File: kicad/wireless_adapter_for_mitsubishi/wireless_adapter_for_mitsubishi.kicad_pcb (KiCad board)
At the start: 2 copper layers, 75 x 50 mm, 53 parts, among them J1 S05B-PASK-2(LF)(SN), J2 S05B-PASK-2(LF)(SN), J3 GT-USB-7010ASV, U1 ESP32-C6-WROOM-1-N8, U2 TXS0104EPWR, U3 TVS1400DRVR, U4 TVS0500DRVR, U5 TVS1400DRVR, U6 TVS0500DRVR, U7 TPS2121RUXR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

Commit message: Rename some of the KiCad sheets.
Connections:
- net /Power Regulator/Power_Multiplexed renamed /Power System/Power_Multiplexed
- net /Power Regulator/Regulator_Input renamed /Power System/Regulator_Input
- net /Power Regulator/USB_5V renamed /Power System/USB_5V

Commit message: Fix the name of a KiCad sheet.
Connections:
- net /Power System/Power_Multiplexed renamed /Power Subsystem/Power_Multiplexed
- net /Power System/Regulator_Input renamed /Power Subsystem/Regulator_Input
- net /Power System/USB_5V renamed /Power Subsystem/USB_5V

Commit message: Rename some KiCad buses.
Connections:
- net /IU Connector/IU_RX_WA_TX renamed /IU Connector/IU_UART_RX
- net /IU Connector/IU_TX_WA_RX renamed /IU Connector/IU_UART_TX
- net /WR Connector/WR_RX_WA_TX renamed /WR Connector/WR_UART_RX
- net /WR Connector/WR_TX_WA_RX renamed /WR Connector/WR_UART_TX

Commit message: Clean up KiCad schematic.
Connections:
- net /Power Subsystem/Power_Multiplexed renamed /Power Subsystem/Multiplexer_Output
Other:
- board text added: "Wireless Adapter for a Mitsubishi Heat Pump Indoor Unit (Rev: 1.1)"
- board text removed: "Wireless Adapter for a Mitsubishi Heat Pump Indoor Unit"

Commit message: Flatten KiCad schematic.
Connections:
- net /IU Connector/IU_12V7 renamed /IU_12V7
- net /IU Connector/IU_5V renamed /IU_5V
- net /IU Connector/IU_UART_RX renamed Net-(U2-A2)
- net /IU Connector/IU_UART_TX renamed Net-(U2-A1)
- net /Power Subsystem/Multiplexer_Output renamed /Multiplexer_Output
- net /Power Subsystem/Regulator_Input renamed /Regulator_Input
- net /Power Subsystem/USB_5V renamed /USB_5V
- net /WR Connector/WR_UART_RX renamed Net-(U2-A3)
- net /WR Connector/WR_UART_TX renamed Net-(U2-A4)

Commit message: Clean up KiCad schematic.
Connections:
- net Net-(U2-A1) renamed /IU_UART_TX
- net Net-(U2-A2) renamed /IU_UART_RX
- net Net-(U2-A3) renamed /WR_UART_RX
- net Net-(U2-A4) renamed /WR_UART_TX

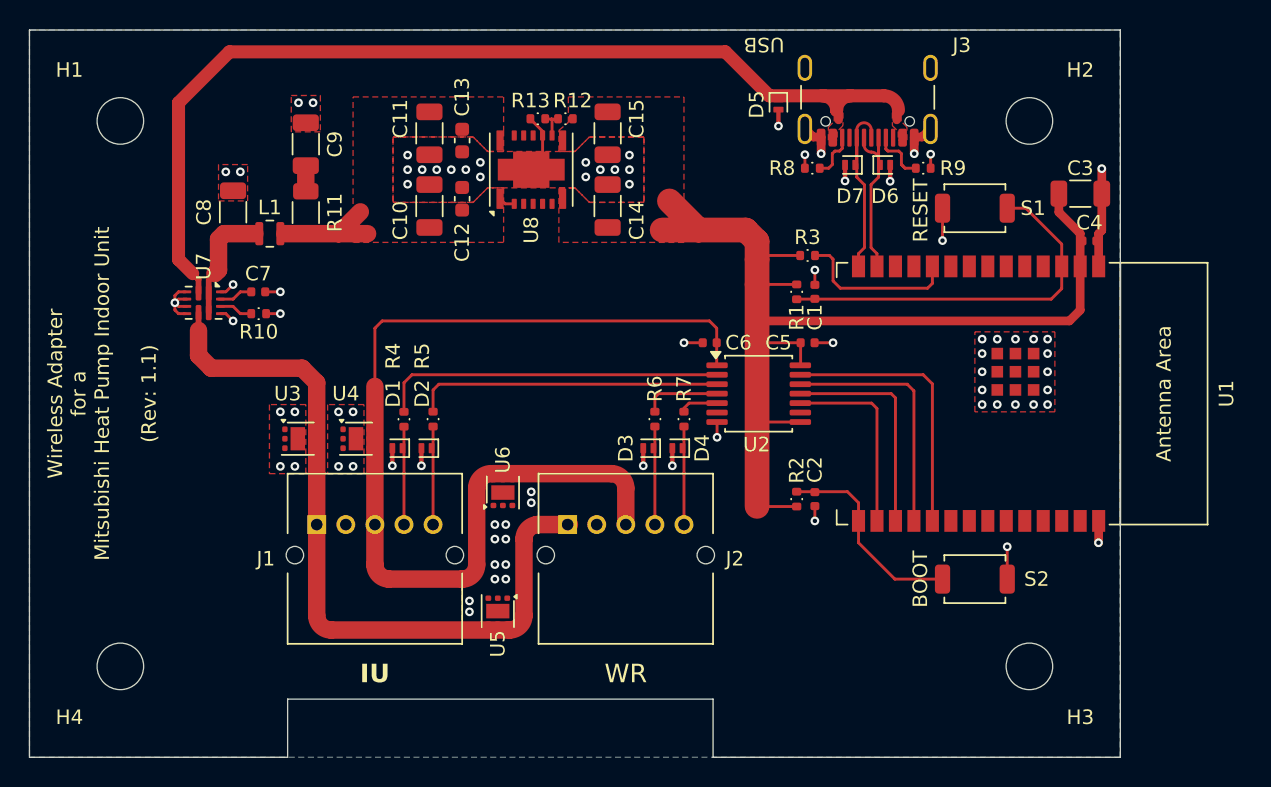
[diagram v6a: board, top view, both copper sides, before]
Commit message: Clean up KiCad schematic. Improve grounding in on PCB.
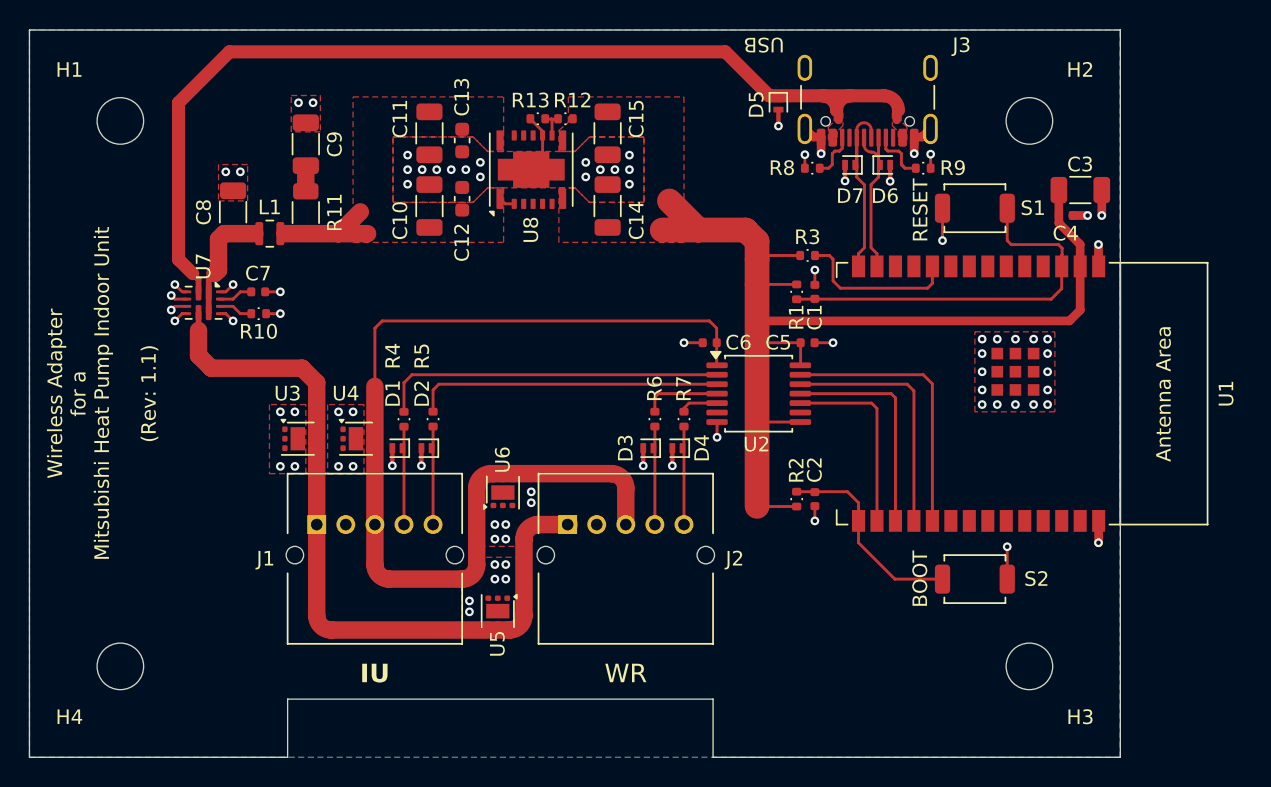
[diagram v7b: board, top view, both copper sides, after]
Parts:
- C2: value 1μF -> 0.1μF
- S1, S2: value SW_SPST -> SW_PUSH
- moved C4 2.39 mm to (171.2, 87.8)
- moved C3 0.25 mm to (172.2, 86.0)
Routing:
- net GND: track 45.3 -> 42.6 mm, vias 81 -> 86
- net /RESET: track 26.3 -> 27.5 mm

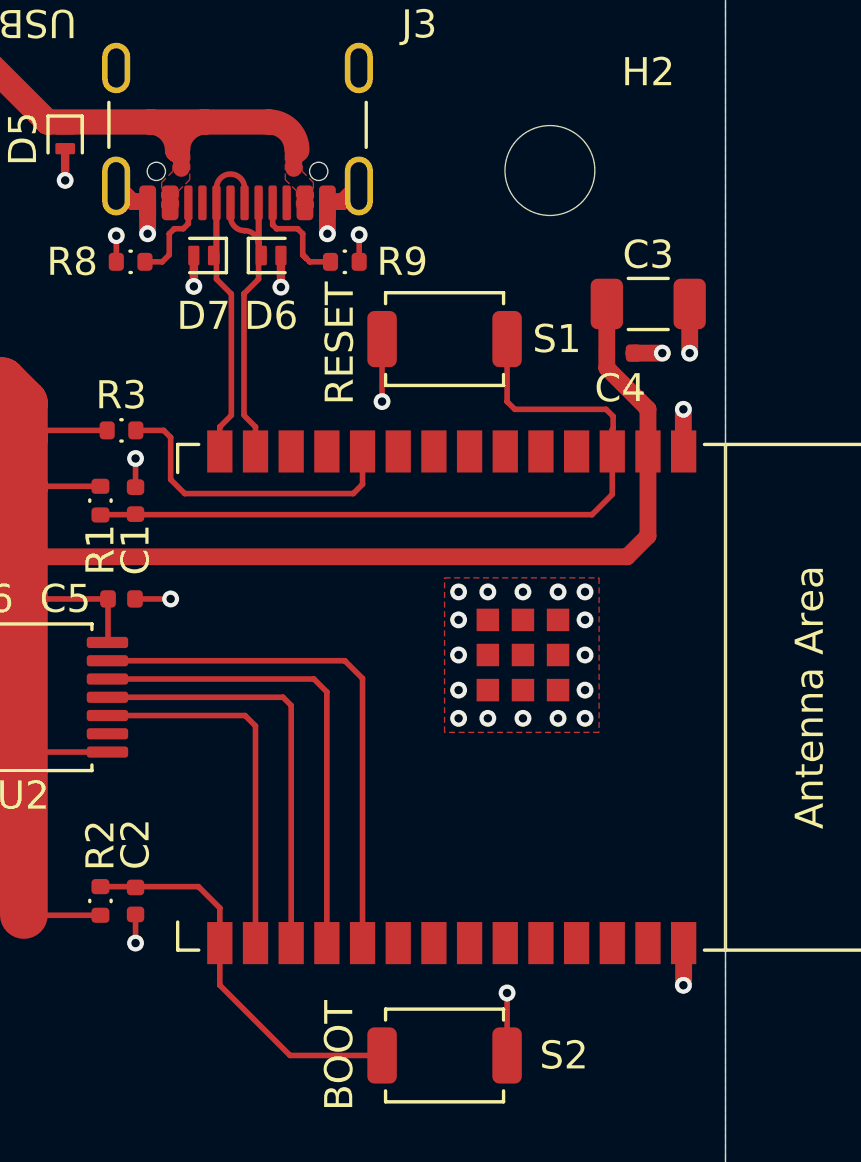
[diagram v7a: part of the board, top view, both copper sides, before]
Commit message: Improve USB differential routing.
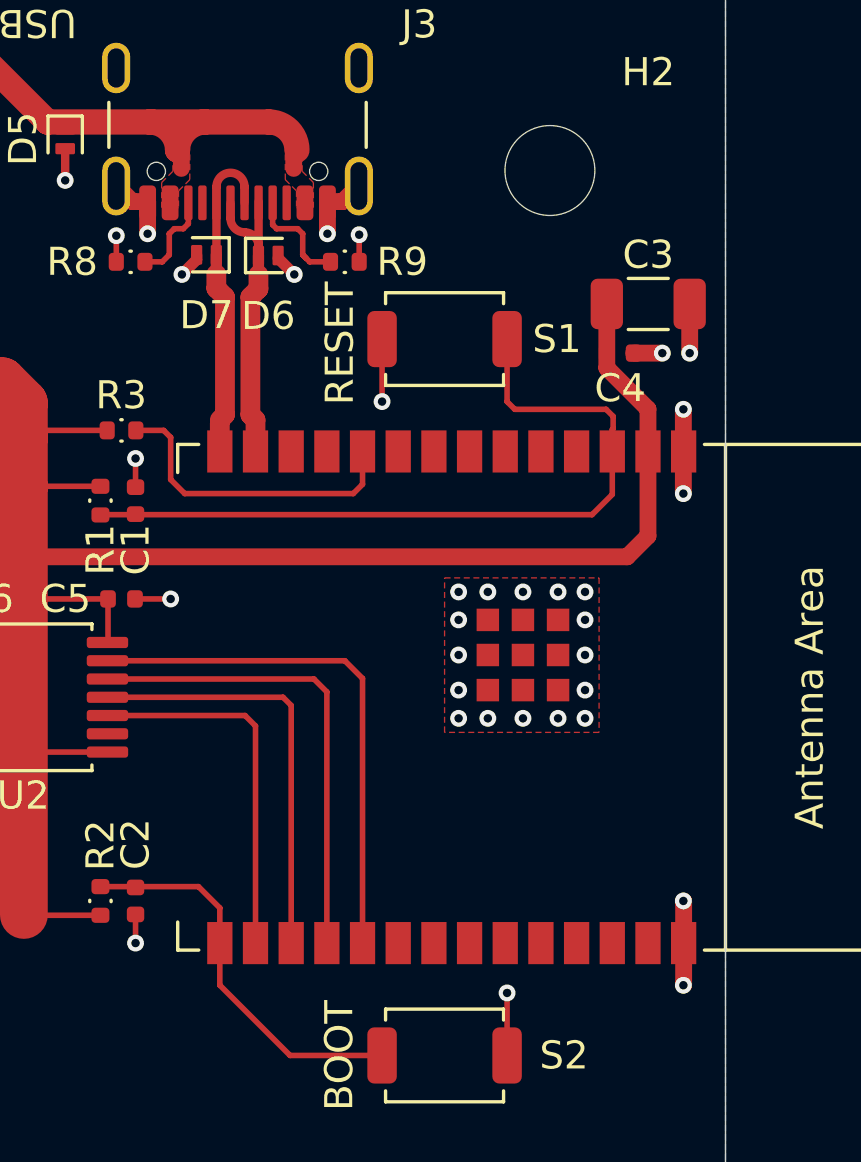
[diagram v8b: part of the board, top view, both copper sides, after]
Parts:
- moved D7 0.10 mm to (156.5, 84.2)
- moved D6 0.10 mm to (158.7, 84.3)
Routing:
- net GND: track 42.6 -> 45.2 mm, vias 86 -> 88
- net /USB_D-: track 13.3 -> 11.1 mm
- net /USB_D+: track 13.5 -> 11.4 mm
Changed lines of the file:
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@@
 	(footprint "Diode_SMD:D_SOD-882"
 		(layer "F.Cu")
-		(at 158.825 84.275)
+		(at 158.725 84.275)
 		(descr "SOD-882, DFN1006-2, body 1.0 x 0.6 x 0.48mm, pitch 0.65mm, https://assets.nexperia.com/documents/package-information/SOD882.pdf")
 		(tags "Diode SOD882 DFN1006-2")
@@
 	(footprint "Diode_SMD:D_SOD-882"
 		(layer "F.Cu")
-		(at 156.425 84.275 180)
+		(at 156.525 84.25 180)
 		(descr "SOD-882, DFN1006-2, body 1.0 x 0.6 x 0.48mm, pitch 0.65mm, https://assets.nexperia.com/documents/package-information/SOD882.pdf")
 		(tags "Diode SOD882 DFN1006-2")
@@
 	)
 	(segment
-		(start 159.175 84.275)
-		(end 159.175 85.4)
-		(width 0.3)
-		(layer "F.Cu")
-		(net "GND")
-	)
-	(segment
 		(start 154 91.5)
 		(end 154 92.52)
@@
 	)
 	(segment
-		(start 156.075 85.375)
-		(end 156.075 84.275)
-		(width 0.3)
-		(layer "F.Cu")
-		(net "GND")
-	)
-	(segment
 		(start 153.985 96.5)
 		(end 155.25 96.5)
@@
 	)
 	(segment
-		(start 173.5 89.75)
-		(end 173.5 91.24)
-		(width 0.6)
+		(start 159.65 84.95)
+		(end 159.075 84.375)
+		(width 0.4)
 		(layer "F.Cu")
 		(net "GND")
@@
 	)
 	(segment
+		(start 155.65 84.95)
+		(end 156.175 84.425)
+		(width 0.4)
+		(layer "F.Cu")
+		(net "GND")
+	)
+	(segment
 		(start 151.495 80.471907)
 		(end 151.495 81.601907)
@@
 	)
 	(segment
+		(start 173.5 107.25)
+		(end 173.51 107.26)
+		(width 0.6)
+		(layer "F.Cu")
+		(net "GND")
+	)
+	(segment
 		(start 144.2 103.75)
 		(end 144.2 104.96)
@@
 	)
 	(segment
+		(start 156.175 84.425)
+		(end 156.175 84.25)
+		(width 0.4)
+		(layer "F.Cu")
+		(net "GND")
+	)
+	(segment
 		(start 113.5 93)
 		(end 114 92.5)
@@
 	)
 	(segment
-		(start 173.51 110.24)
-		(end 173.5 110.25)
-		(width 0.6)
-		(layer "F.Cu")
-		(net "GND")
-	)
-	(segment
 		(start 171.73 87.75)
 		(end 172.75 87.75)
@@
 	)
 	(segment
-		(start 173.51 108.75)
-		(end 173.51 110.24)
-		(width 0.6)
-		(layer "F.Cu")
-		(net "GND")
-	)
-	(segment
 		(start 167.225 110.525)
 		(end 167.225 112.75)
@@
 	)
 	(segment
+		(start 173.51 110.24)
+		(end 173.5 110.25)
+		(width 0.6)
+		(layer "F.Cu")
+		(net "GND")
+	)
+	(segment
 		(start 135.28 82.25)
 		(end 135.28 83.48)
@@
 	)
 	(segment
+		(start 173.5 89.75)
+		(end 173.5 92.75)
+		(width 0.6)
+		(layer "F.Cu")
+		(net "GND")
+	)
+	(segment
 		(start 124.95 104.96)
 		(end 124.95 103.75)
@@
 		(net "GND")
 	)
+	(segment
+		(start 173.51 107.26)
+		(end 173.51 110.24)
+		(width 0.6)
+		(layer "F.Cu")
+		(net "GND")
+	)
 	(via
 		(at 167.79 100.75)
@@
 	)
 	(via
+		(at 173.5 92.75)
+		(size 0.6)
+		(drill 0.3)
+		(layers "F.Cu" "B.Cu")
+		(free yes)
+		(net "GND")
+	)
+	(via
 		(at 130 84.6)
 		(size 0.6)
@@
 	)
 	(via
-		(at 156.075 85.375)
+		(at 155.65 84.95)
 		(size 0.6)
 		(drill 0.3)
@@
 	)
 	(via
-		(at 159.175 85.4)
+		(at 159.65 84.95)
 		(size 0.6)
 		(drill 0.3)
@@
 	)
 	(via
+		(at 173.5 107.25)
+		(size 0.6)
+		(drill 0.3)
+		(layers "F.Cu" "B.Cu")
+		(free yes)
+		(net "GND")
+	)
+	(via
 		(at 173.725 87.75)
 		(size 0.6)
@@
 	)
 	(segment
-		(start 157.86 85.635)
-		(end 157.86 89.934405)
-		(width 0.2)
+		(start 158.38 82.355)
+		(end 158.38 84.17)
+		(width 0.3)
 		(layer "F.Cu")
 		(net "/USB_D-")
 	)
 	(segment
-		(start 158.38 82.355)
-		(end 158.38 85.115)
-		(width 0.2)
+		(start 158.375 84.96245)
+		(end 158.375 85.46245)
+		(width 0.7049)
 		(layer "F.Cu")
 		(net "/USB_D-")
 	)
 	(segment
-		(start 158.27 90.374999)
-		(end 157.86 89.964999)
-		(width 0.2)
+		(start 158.08745 85.75)
+		(end 158.08745 89.942449)
+		(width 0.7049)
 		(layer "F.Cu")
 		(net "/USB_D-")
 	)
 	(segment
-		(start 158.38 84.6)
-		(end 158.38 82.355)
-		(width 0.2)
+		(start 158.27 90.124999)
+		(end 158.27 91.25)
+		(width 0.7049)
 		(layer "F.Cu")
 		(net "/USB_D-")
 	)
 	(segment
-		(start 158.27 91.5)
-		(end 158.27 90.374999)
-		(width 0.2)
+		(start 157.38 82.95)
+		(end 157.38 82.4)
+		(width 0.3)
 		(layer "F.Cu")
 		(net "/USB_D-")
 	)
 	(segment
-		(start 158.38 85.115)
-		(end 157.86 85.635)
-		(width 0.2)
+		(start 158.375 84.275)
+		(end 158.375 84.96245)
+		(width 0.4)
+		(layer "F.Cu")
+		(net "/USB_D-")
+	)
+	(segment
+		(start 158.08745 89.942449)
+		(end 158.27 90.124999)
+		(width 0.7049)
+		(layer "F.Cu")
+		(net "/USB_D-")
+	)
+	(segment
+		(start 158.375 85.46245)
+		(end 158.08745 85.75)
+		(width 0.7049)
 		(layer "F.Cu")
 		(net "/USB_D-")
 	)
 	(arc
-		(start 157.88 83.39)
-		(mid 158.233553 83.536447)
-		(end 158.38 83.89)
-		(width 0.2)
+		(start 157.88 83.45)
+		(mid 157.526447 83.303553)
+		(end 157.38 82.95)
+		(width 0.3)
 		(layer "F.Cu")
 		(net "/USB_D-")
 	)
 	(arc
-		(start 157.88 83.39)
-		(mid 157.526447 83.243553)
-		(end 157.38 82.89)
-		(width 0.2)
+		(start 157.88 83.45)
+		(mid 158.233553 83.596447)
+		(end 158.38 83.95)
+		(width 0.3)
 		(layer "F.Cu")
 		(net "/USB_D-")
 	)
 	(segment
-		(start 157.41 89.964999)
-		(end 157 90.374999)
-		(width 0.2)
+		(start 157 90.25)
+		(end 157 91.25)
+		(width 0.7049)
 		(layer "F.Cu")
 		(net "/USB_D+")
 	)
 	(segment
-		(start 157 90.374999)
-		(end 157 91.5)
-		(width 0.2)
+		(start 156.875 84.94245)
+		(end 156.875 85.44245)
+		(width 0.7049)
 		(layer "F.Cu")
 		(net "/USB_D+")
 	)
 	(segment
-		(start 157.41 85.645)
-		(end 157.41 89.934405)
-		(width 0.2)
+		(start 156.88 81.83)
+		(end 156.88 84.155)
+		(width 0.3)
 		(layer "F.Cu")
 		(net "/USB_D+")
 	)
 	(segment
-		(start 156.88 84.55)
-		(end 156.88 82.355)
-		(width 0.2)
+		(start 157.18255 89.942449)
+		(end 157 90.124999)
+		(width 0.7049)
 		(layer "F.Cu")
 		(net "/USB_D+")
 	)
 	(segment
-		(start 156.88 82.355)
-		(end 156.88 85.115)
-		(width 0.2)
+		(start 156.875 84.94245)
+		(end 156.875 84.25)
+		(width 0.4)
 		(layer "F.Cu")
 		(net "/USB_D+")
 	)
 	(segment
-		(start 156.88 85.115)
-		(end 157.41 85.645)
-		(width 0.2)
+		(start 157.18255 85.75)
+		(end 157.18255 89.942449)
+		(width 0.7049)
 		(layer "F.Cu")
 		(net "/USB_D+")
 	)
 	(segment
-		(start 156.88 84.195001)
-		(end 156.88 84.55)
-		(width 0.2)
+		(start 156.875 85.44245)
+		(end 157.18255 85.75)
+		(width 0.7049)
+		(layer "F.Cu")
+		(net "/USB_D+")
+	)
+	(segment
+		(start 157.88 81.83)
+		(end 157.88 82.4)
+		(width 0.3)
 		(layer "F.Cu")
 		(net "/USB_D+")
 	)
 	(arc
-		(start 156.88 81.875)
-		(mid 157.38 81.375)
-		(end 157.88 81.875)
-		(width 0.2)
+		(start 156.88 81.83)
+		(mid 157.38 81.33)
+		(end 157.88 81.83)
+		(width 0.3)
 		(layer "F.Cu")
 		(net "/USB_D+")
@@
 		(net "GND")
 		(layer "F.Cu")
+		(name "WR_12V7_TVS")
 		(hatch edge 0.5)
 		(priority 8)
@@
 		(net "GND")
 		(layer "F.Cu")
+		(name "EMI_FILTER_IN")
 		(hatch edge 0.5)
 		(priority 7)
@@
 		(net "GND")
 		(layer "F.Cu")
-		(name "REGULATOR_INPUT")
+		(name "ESP32_THERMAL_PAD")
 		(hatch edge 0.5)
 		(priority 4)
@@
 		(net "/USB_5V")
 		(layer "F.Cu")
+		(name "USB_5V_B4")
 		(hatch edge 0.5)
 		(priority 2)
@@
 		(net "GND")
 		(layer "F.Cu")
+		(name "WR_5V_TVS")
 		(hatch edge 0.5)
 		(priority 5)
@@
 		(net "GND")
 		(layer "F.Cu")
+		(name "EMI_FILTER_OUT")
 		(hatch edge 0.5)
 		(priority 6)
@@
 		(net "GND")
 		(layer "F.Cu")
-		(name "REGULATOR_INPUT")
+		(name "IU_12V7_TVS")
 		(hatch edge 0.5)
 		(priority 3)
@@
 		(net "GND")
 		(layer "F.Cu")
-		(name "REGULATOR_INPUT")
+		(name "IU_5V_TVS")
 		(hatch edge 0.5)
 		(priority 3)
@@
 		(net "/USB_5V")
 		(layer "F.Cu")
+		(name "USB_5V_A4")
 		(hatch edge 0.5)
 		(priority 2)
@@
 		(net "GND")
 		(layer "B.Cu")
+		(name "GROUND_PLANE")
 		(hatch edge 0.5)
 		(connect_pads
